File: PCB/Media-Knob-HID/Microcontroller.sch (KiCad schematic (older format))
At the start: 25 parts, among them IC1 Atmega32U4, J1 TC2030_IDC_Atmel, J2 2x3_254, Q1 16MHz_KX_7

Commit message: Umbau auf mehrere Platinen
Umbau auf 2 Paltinen
- HID Paltine
- USB Platine
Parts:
- removed J1: TC2030_IDC_Atmel, Stecker:TC_2030_IDC_NL, symbol Stecker:TC2030_IDC_Atmel
- renumbered C14 to C10, C15 to C11, C16 to C12, C7 to C3, C8 to C4, C9 to C5, C10 to C6, C11 to C7, C12 to C8, C13 to C9, IC1 to IC3, J2 to J5, R1 to R3, R2 to R4, R3 to R5, R4 to R6, TP5 to TP1, TP6 to TP2, TP7 to TP3, TP8 to TP4, TP9 to TP5, TP10 to TP6, TP11 to TP7
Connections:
- net labels added: +3.3V
- net labels removed: VCC
- wire segments 106 -> 100

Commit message: Interface und Powersupply
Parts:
- added TP406: TP_100, Technik:TP100_VIA030_PAD100, symbol Technik:TP_100
- renumbered C3 to C401, C4 to C402, C5 to C403, C6 to C404, C7 to C405, C8 to C406, C9 to C407, C10 to C408, C11 to C409, C12 to C410, IC3 to IC401, J5 to J401, Q1 to Q401, R3 to R401, R4 to R402, R5 to R403, R6 to R404, TP1 to TP401, TP2 to TP402, TP3 to TP403, TP4 to TP404, TP5 to TP405, TP6 to TP407, TP7 to TP408
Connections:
- net Input_Select: now also TP406.1
- net Output_Select: no longer names the net of IC401.29 (PB5_(PCINT5/OC1A/~OC4B~/ADC12))
- no-connect marks 10 -> 11
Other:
- moved on the sheet: C401, C402, C403, C404, C405, C406, C407, C408, C409, C410, IC401, J401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

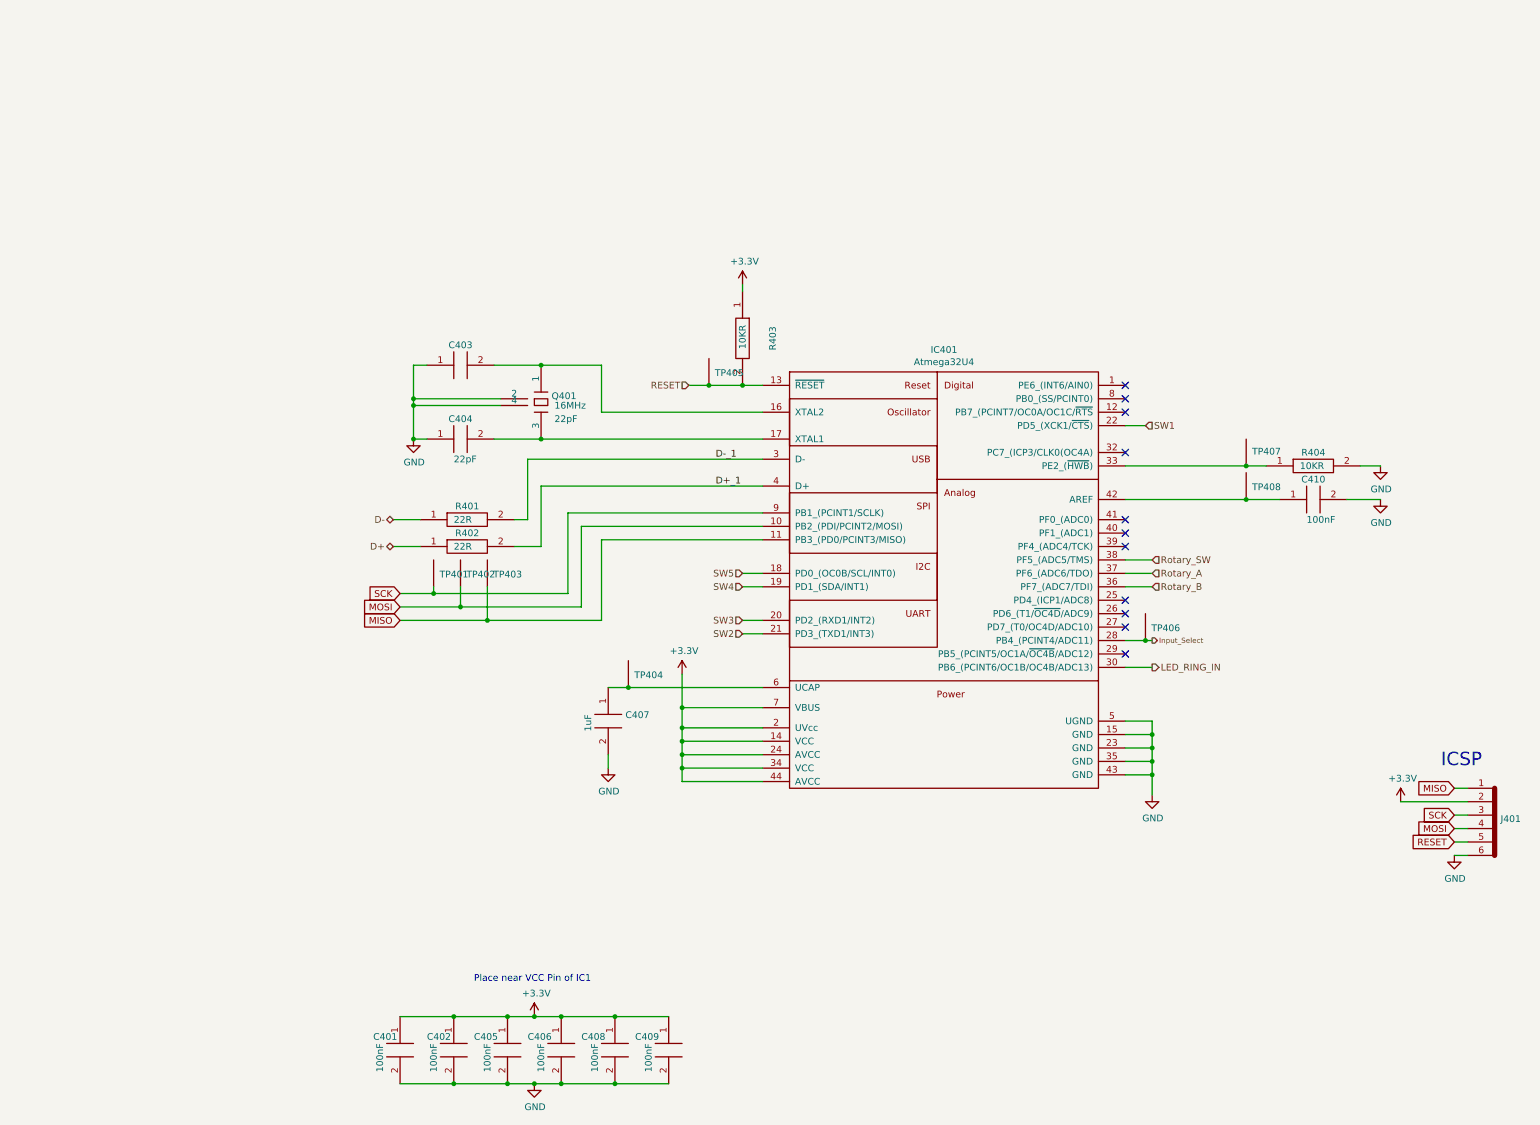
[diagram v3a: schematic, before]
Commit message: Media_knob an neues Konzept angepasst
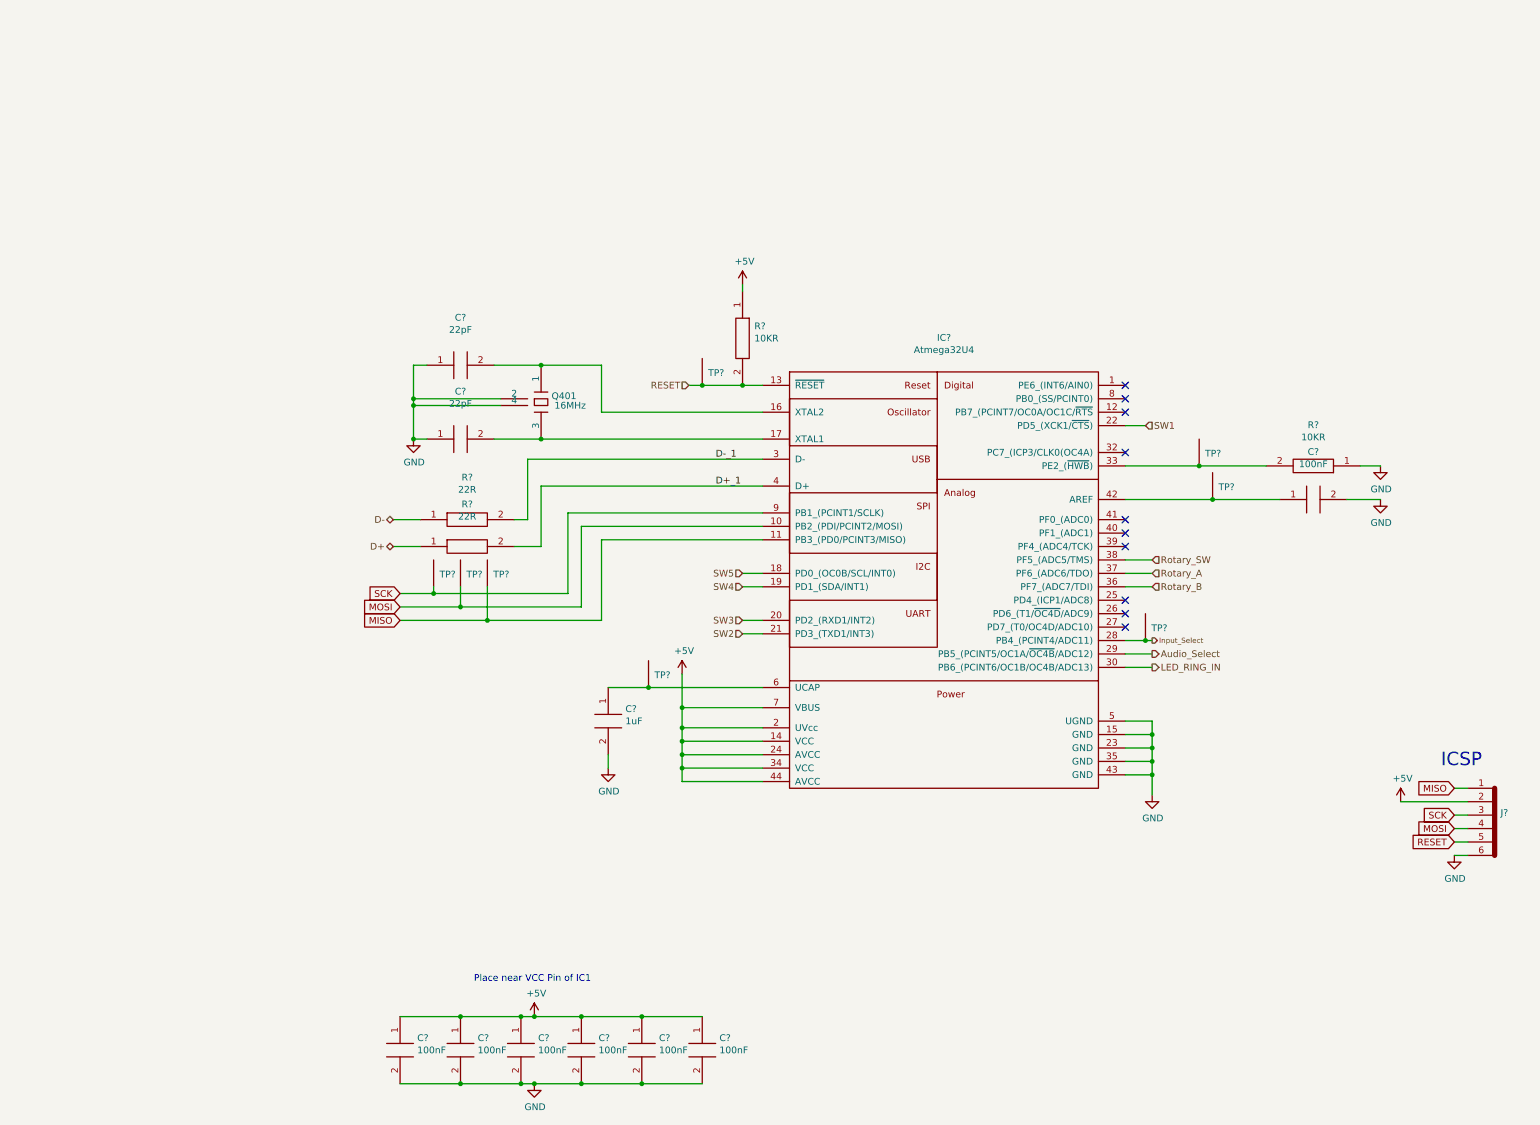
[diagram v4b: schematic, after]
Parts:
- removed C401, C402, C405, C406, C408, C409, C410: 100n_0603, Kondensator:CAPC1608, symbol Kondensator:100n_0603
- removed C403, C404: 22p_0603, Kondensator:CAPC1608, symbol Kondensator:22p_0603
- removed C407: 1u_0603, Kondensator:CAPC1608, symbol Kondensator:1u_0603
- removed IC401: Atmega32U4, Microcontroller:ATMEGA32U4-AU, symbol Mikrocontroller:Atmega32U4
- removed J401: 2x3_254, Stecker:2x3_254, symbol Stecker:2x3_254
- removed R401, R402: 22R_0603, Widerstand:RESC1608, symbol Widerstand:22R_0603
- removed R403, R404: 10K_0603, Widerstand:RESC1608, symbol Widerstand:10K_0603
- removed TP401, TP402: TP_100, Technik:TP100, symbol Technik:TP_100
- removed TP403, TP404, TP405, TP406, TP407, TP408: TP_100, Technik:TP100_VIA030_PAD100, symbol Technik:TP_100
- added C? (x7): 100n_0603, Kondensator:CAPC1608, symbol _Kondensator:100n_0603
- added C? (x2): 22p_0603, Kondensator:CAPC1608, symbol _Kondensator:22p_0603
- added C?: 1u_0603, Kondensator:CAPC1608, symbol _Kondensator:1u_0603
- added IC?: Atmega32U4, Microcontroller:ATMEGA32U4-AU, symbol _Mikrocontroller:Atmega32U4
- added J?: 2x3_254, Stecker:2x3_254, symbol _Stecker:2x3_254
- added R? (x2): 22R_0603, Widerstand:RESC1608, symbol _Widerstand:22R_0603
- added R? (x2): 10K_0603, Widerstand:RESC1608, symbol _Widerstand:10K_0603
- added TP? (x8): TP_100, Technik:TP100;, symbol _Technik:TP_100
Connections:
- net D+: now also R?.1
- net D+_1: now also IC?.4 (D+), R?.2
- net D-: now also R?.1
- net D-_1: now also IC?.3 (D-), R?.2
- net GND: now also C?.1, C?.1, C?.2, C?.2, C?.2, C?.2, C?.2, C?.2, C?.2, C?.2, IC?.15 (GND), IC?.23 (GND), IC?.35 (GND), IC?.43 (GND), IC?.5 (UGND), J?.6, R?.1
- net Input_Select: now also IC?.28 (PB4_(PCINT4/ADC11)), TP?.1
- net LED_RING_IN: now also IC?.30 (PB6_(PCINT6/OC1B/OC4B/ADC13))
- net MISO: now also IC?.11 (PB3_(PD0/PCINT3/MISO)), J?.1, TP?.1
- net MOSI: now also IC?.10 (PB2_(PDI/PCINT2/MOSI)), J?.4, TP?.1
- net RESET: now also IC?.13 (~RESET~), J?.5, R?.2, TP?.1
- net Rotary_A: now also IC?.37 (PF6_(ADC6/TDO))
- net Rotary_B: now also IC?.36 (PF7_(ADC7/TDI))
- net Rotary_SW: now also IC?.38 (PF5_(ADC5/TMS))
- net SCK: now also IC?.9 (PB1_(PCINT1/SCLK)), J?.3, TP?.1
- net SW1: now also IC?.22 (PD5_(XCK1/~CTS~))
- net SW2: now also IC?.21 (PD3_(TXD1/INT3))
- net SW3: now also IC?.20 (PD2_(RXD1/INT2))
- net SW4: now also IC?.19 (PD1_(SDA/INT1))
- net SW5: now also IC?.18 (PD0_(OC0B/SCL/INT0))
- net at Q401.1: now also C?.2, IC?.16 (XTAL2)
- net at Q401.3: now also C?.2, IC?.17 (XTAL1)
- new net: IC?.33 (PE2_(~HWB~)), R?.2, TP?.1
- new net: C?.1, IC?.42 (AREF), TP?.1
- new net: C?.1, IC?.6 (UCAP), TP?.1
- new net +5V: C?.1, C?.1, C?.1, C?.1, C?.1, C?.1, IC?.14 (VCC), IC?.2 (UVcc), IC?.24 (AVCC), IC?.34 (VCC), IC?.44 (AVCC), IC?.7 (VBUS), J?.2, R?.1
- new net Audio_Select: IC?.29 (PB5_(PCINT5/OC1A/~OC4B~/ADC12))
- no-connect marks 11 -> 10
